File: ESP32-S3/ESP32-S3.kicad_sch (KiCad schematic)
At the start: 58 parts, among them J1 POWER, J10 JTAG, J2 USB_C_Receptacle_USB2.0_16P, J3 USB_C_Receptacle_USB2.0_16P, J4 JTAG, J5 JTAG, J6 SPI, J7 SERVO_1, J8 SERVO_1, J9 I2C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

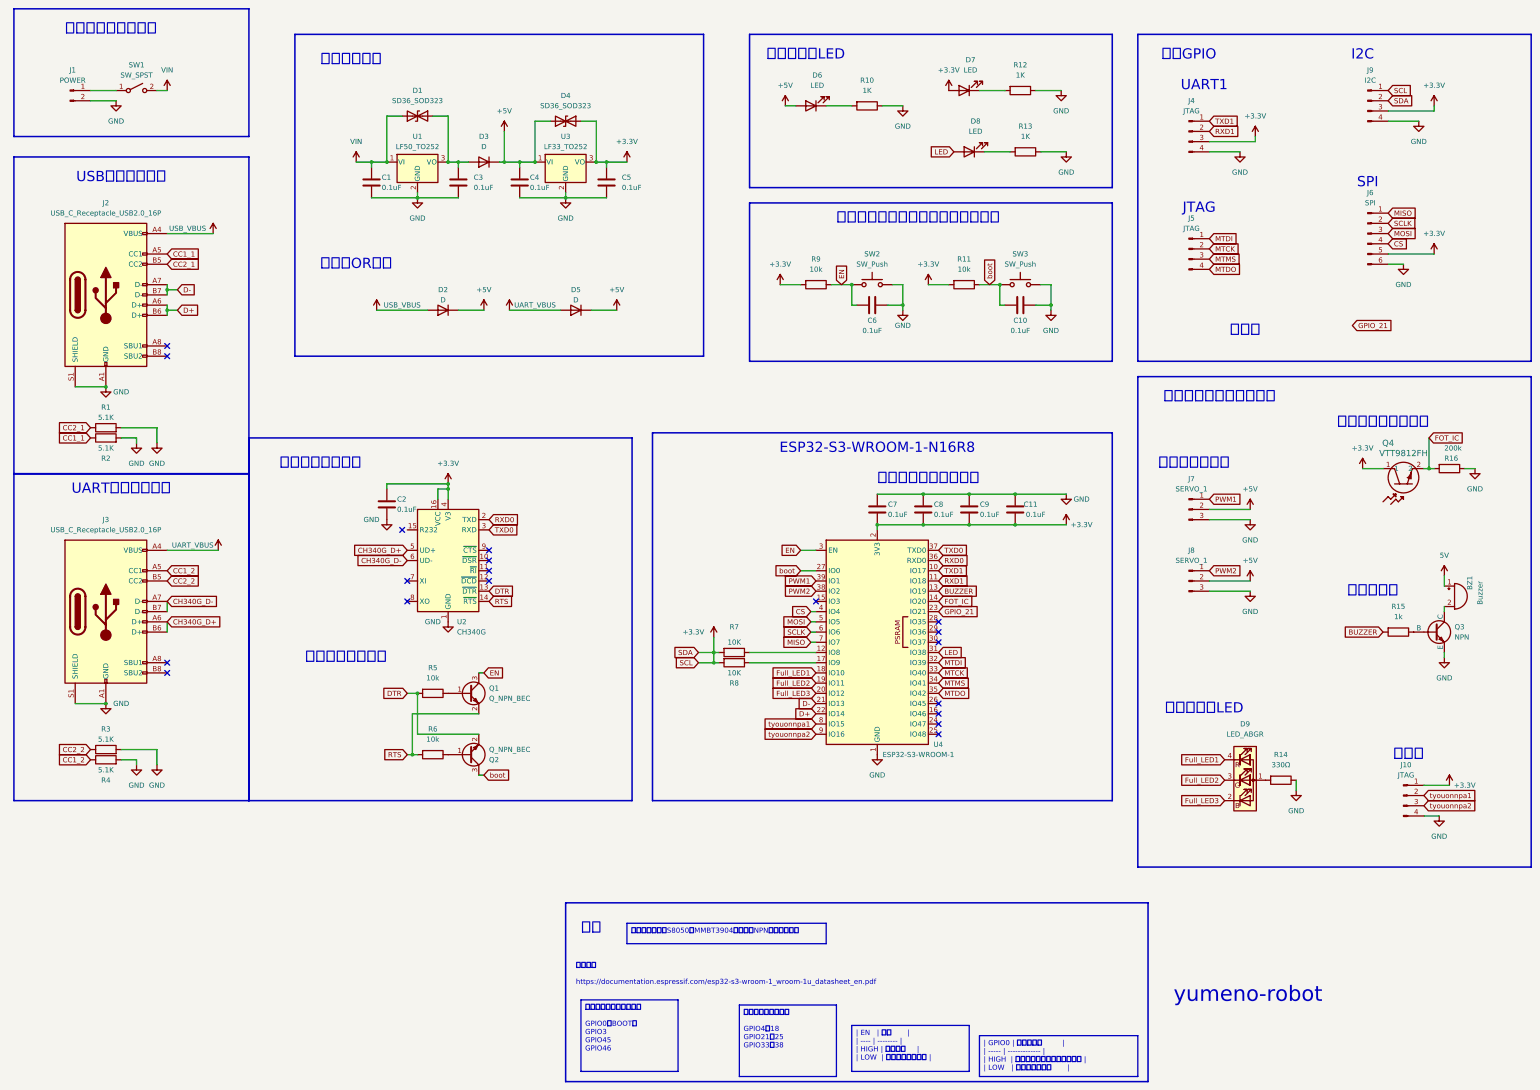
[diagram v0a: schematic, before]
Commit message: クロック回路の追加
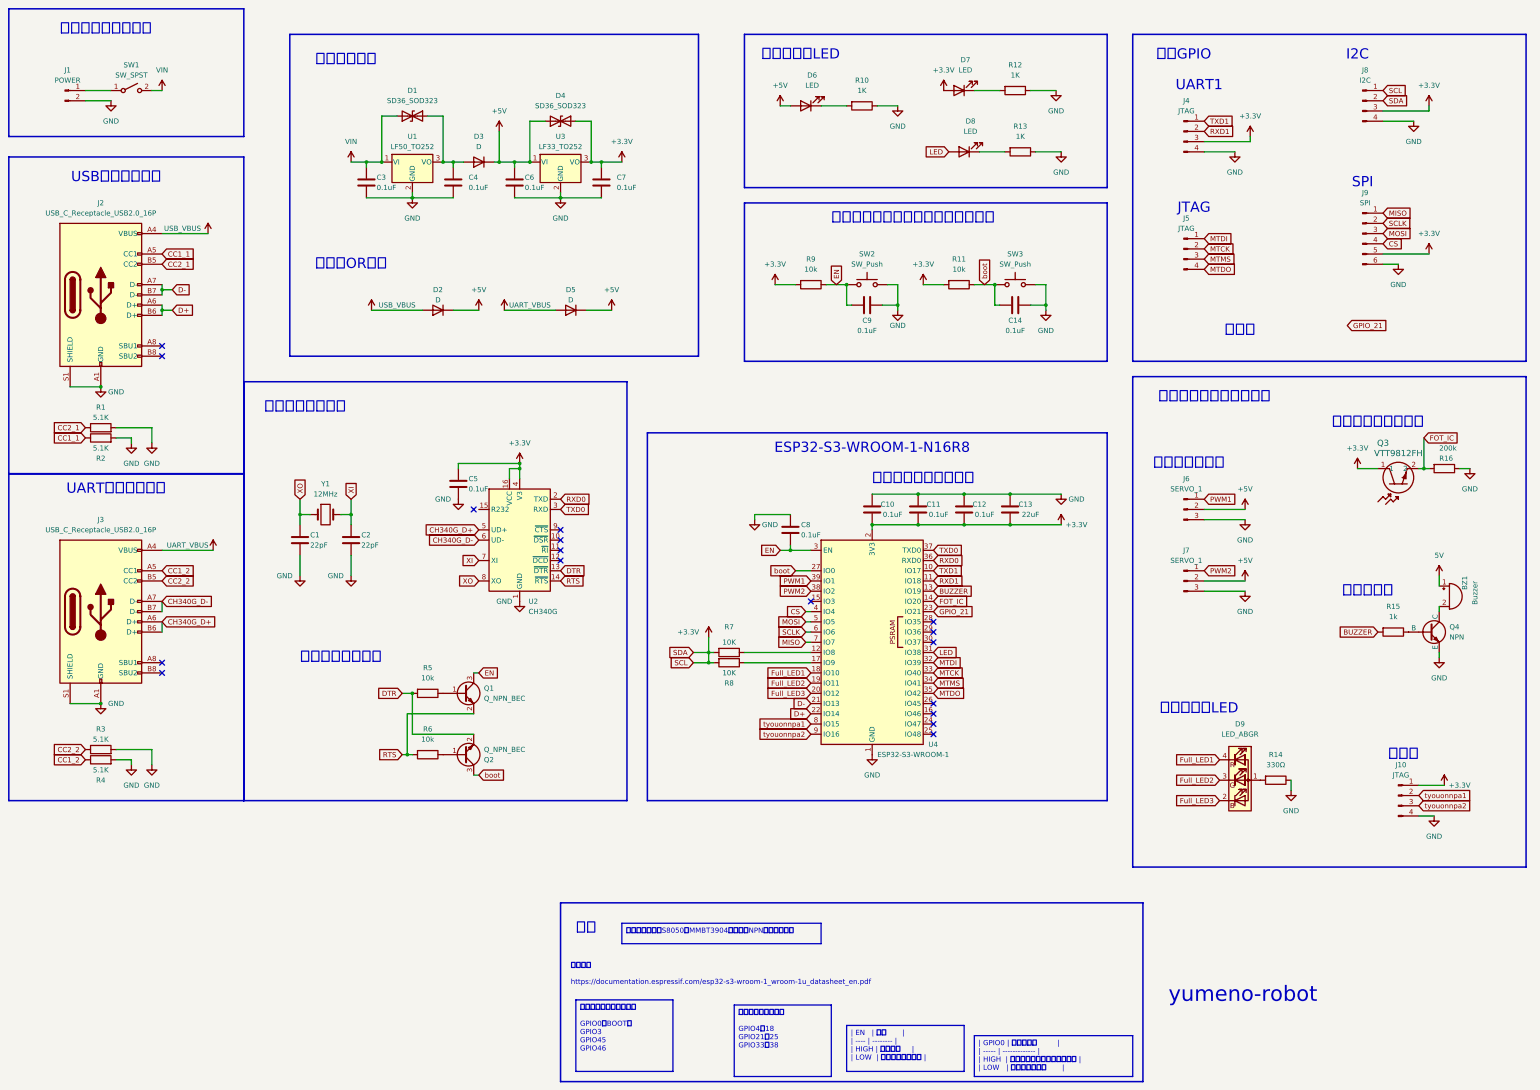
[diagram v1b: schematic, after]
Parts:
- removed J6: SPI, symbol Connector:Conn_01x06_Pin
- removed J8: SERVO_1, symbol Connector:Conn_01x03_Pin
- removed J9: I2C, symbol Connector:Conn_01x04_Pin
- removed Q3: NPN, Package_TO_SOT_SMD:TSOT-23, symbol Simulation_SPICE:NPN
- removed Q4: VTT9812FH, yumenorobot:NJL7502R, symbol robocup:VTT9812FH
- added C12, C14: 0.1uF, symbol Device:C
- added C13: 22uF, symbol Device:C
- added J6: SERVO_1, symbol Connector:Conn_01x03_Pin
- added J8: I2C, symbol Connector:Conn_01x04_Pin
- added J9: SPI, symbol Connector:Conn_01x06_Pin
- added Q3: VTT9812FH, yumenorobot:NJL7502R, symbol robocup:VTT9812FH
- added Q4: NPN, Package_TO_SOT_SMD:TSOT-23, symbol Simulation_SPICE:NPN
- added Y1: 12MHz, symbol Device:Crystal
- C1, C2: value 0.1uF -> 22pF
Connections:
- net +3.3V: now also C10.1, C12.1, C13.1, J8.1 (Pin_1), J8.2 (Pin_2), J8.3 (Pin_3), J9.5 (Pin_5), Q3.1; no longer C2.1, C8.1, C9.1
- net +5V: now also C6.1, J6.2 (Pin_2); no longer C4.1
- net CS: now also J9.4 (Pin_4)
- net EN: now also C8.1, C9.1; no longer C6.1
- net FOT_IC: now also Q3.2
- net GND: now also C12.2, C13.2, C14.2, J6.3 (Pin_3), J8.4 (Pin_4), J9.6 (Pin_6), Q4.3 (E)
- net MISO: now also J9.1 (Pin_1)
- net MOSI: now also J9.3 (Pin_3)
- net PWM1: now also J6.1 (Pin_1); no longer J7.1 (Pin_1)
- net PWM2: now also J7.1 (Pin_1)
- net SCLK: now also J9.2 (Pin_2)
- net VIN: now also C3.1; no longer C1.1
- net boot: now also C14.1; no longer C10.1
- net at D1.2 (A2), D3.2 (A), U1.3 (VO): now also C4.1; no longer C3.1
- net at R15.1: now also Q4.2 (B)
- net at BZ1.2 (-): now also Q4.1 (C)
- net XI: now reaches U2.7 (XI)
- net XI: now also C2.1, Y1.2
- net XO: now reaches U2.8 (XO)
- net XO: now also C1.1, Y1.1
- no-connect marks 19 -> 17
